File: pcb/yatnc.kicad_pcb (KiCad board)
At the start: 2 copper layers, 55 x 85 mm, 44 parts, among them J1 Conn_02x03_Top_Bottom, J2 JST, J3 Conn_01x02_Socket, J4 DFR0570, J5 Conn_01x13_Socket, J6 Conn_01x13_Socket, Q1 BC547, Q2 BC547, SW1 RST, U1 MAX3232

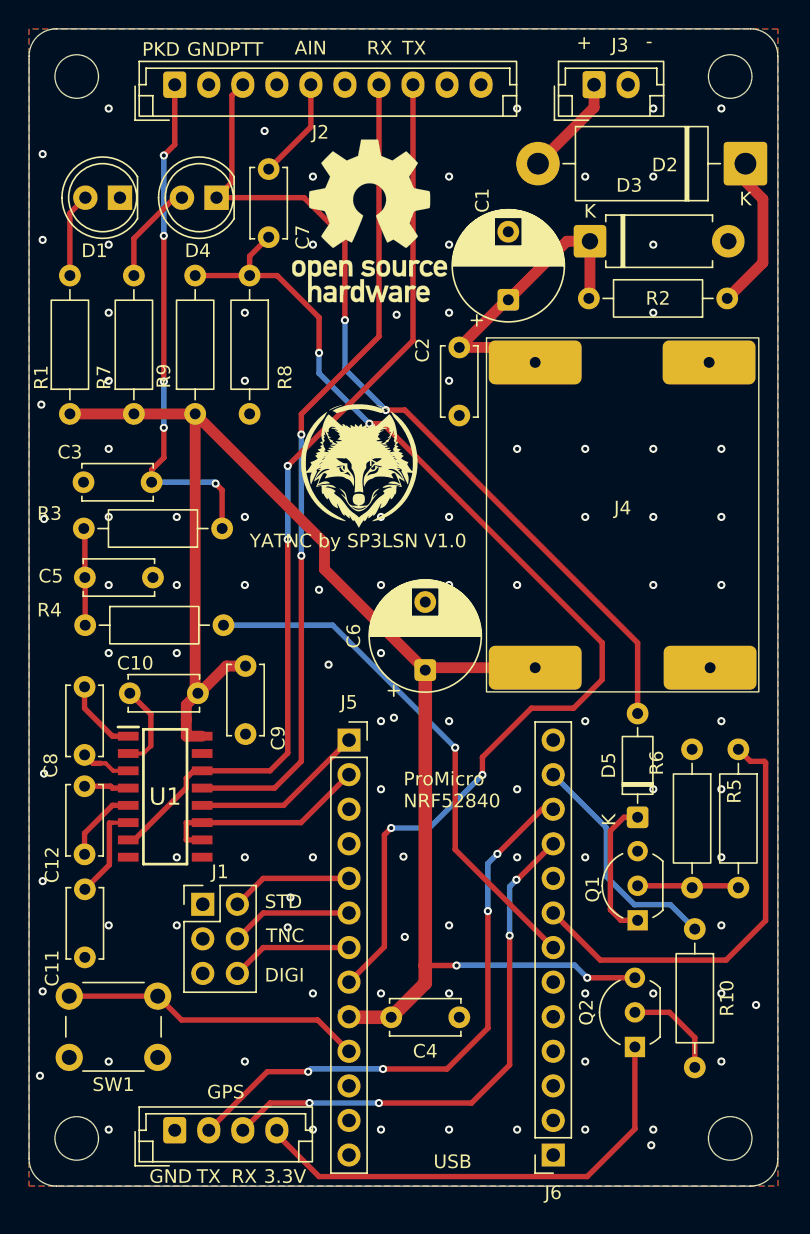
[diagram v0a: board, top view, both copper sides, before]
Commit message: max3232 refactor
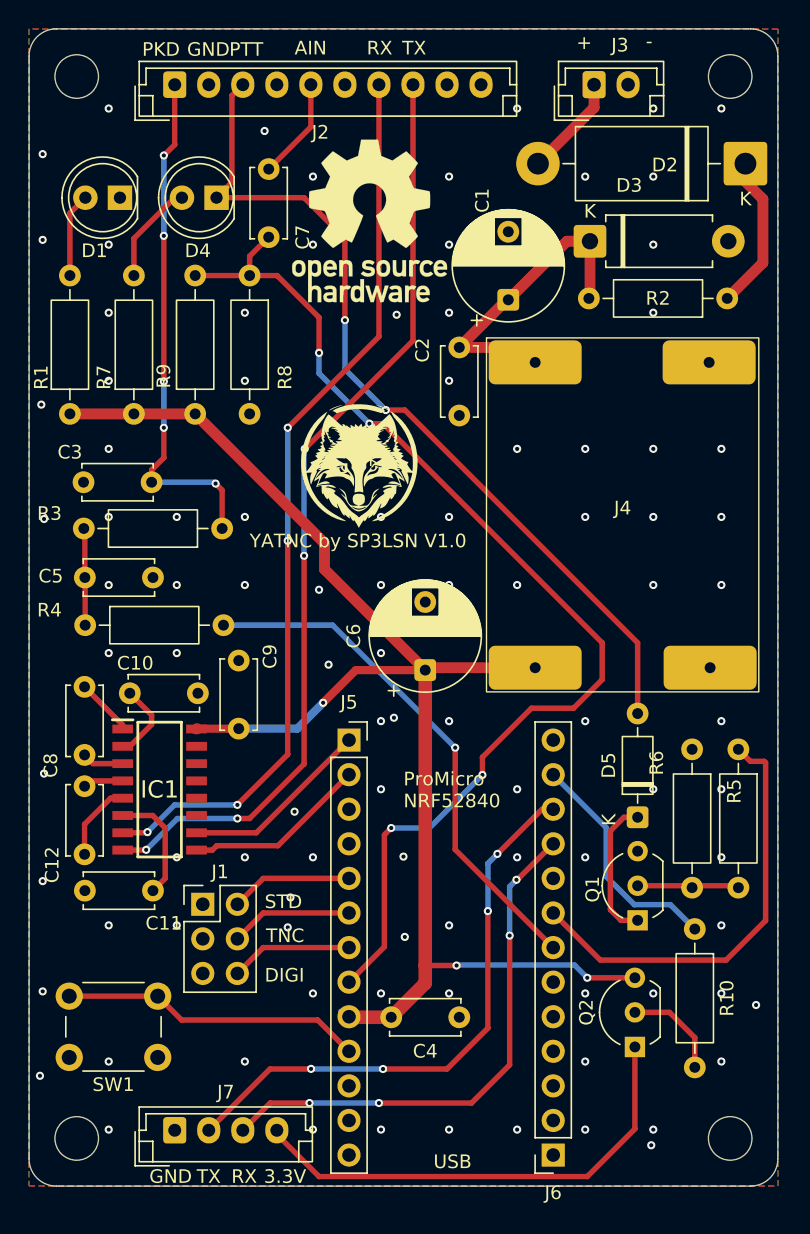
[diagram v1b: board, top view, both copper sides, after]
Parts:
- removed U1: MAX3232, liby:SOIC127P600X175-16N
- added IC1: MAX3232CDR, liby:SOIC127P600X175-16N, F.Cu at (180.1, 102.4)
- J7: renamed from GPS; value GPS -> Conn_01x04_Pin
- moved C9 4.63 mm to (185.9, 97.9), turned to 90 degrees
- moved C11 0.10 mm to (174.6, 109.8), turned to 0 degrees
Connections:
- net Net-(J6-Pin_8) renamed PTT ON
- C10 pad 2: 3.3V -> GND
- C11 pad 1: Net-(U1-VS-) -> GND
- C11 pad 2: GND -> Net-(IC1-V-)
- J5 pad 1: Net-(J5-Pin_1) -> U0_RX
- J5 pad 2: Net-(J5-Pin_2) -> U0_TX
- J6 pad 4: unconnected-(J6-Pin_4-Pad4) -> GND
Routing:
- net Net-(J5-Pin_2): track 15.8 -> 0.00 mm
- net U0_RX: track 0.00 -> 14.2 mm
- net U0_TX: track 0.00 -> 13.5 mm
- net Net-(J5-Pin_1): track 12.8 -> 0.00 mm
- net 3.3V: track 118.9 -> 107.9 mm, vias 2 -> 3
- net Net-(IC1-V-): track 0.00 -> 8.48 mm
- net Net-(U1-VS-): track 7.03 -> 0.00 mm
- net RX: track 60.2 -> 66.5 mm, vias 2 -> 4
- net TX: track 67.7 -> 69.2 mm, vias 2 -> 4
- net Net-(IC1-C1+): track 5.64 -> 4.26 mm
- net Net-(IC1-V+): track 6.41 -> 5.75 mm
- net Net-(IC1-C1-): track 3.69 -> 3.07 mm
- net GND: track 0.00 -> 0.38 mm, vias 99 -> 100

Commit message: final polish before test order
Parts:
- TO TRCV: renamed from J2
- renumbered J3 to PWR
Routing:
- net GND: vias 100 -> 99

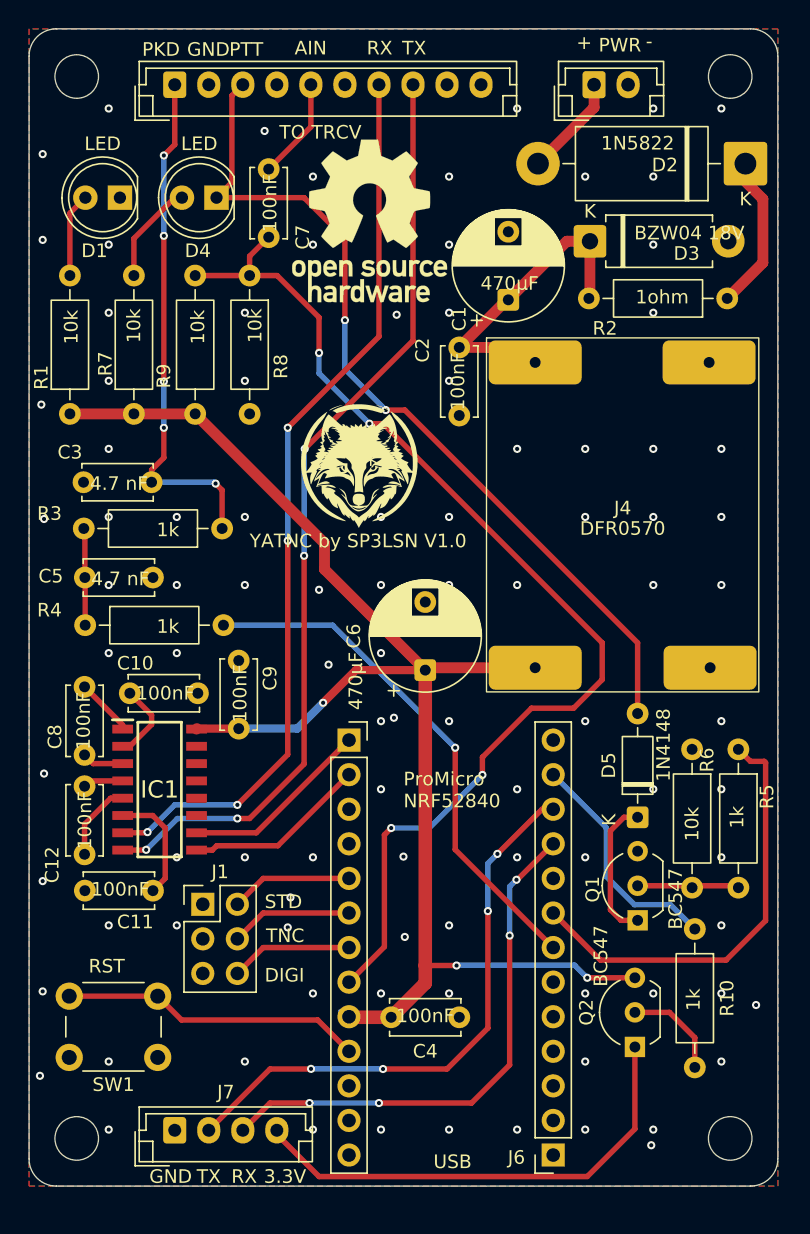
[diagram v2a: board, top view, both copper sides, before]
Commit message: small tweaks on silkscreen side, change components. update README, add bom
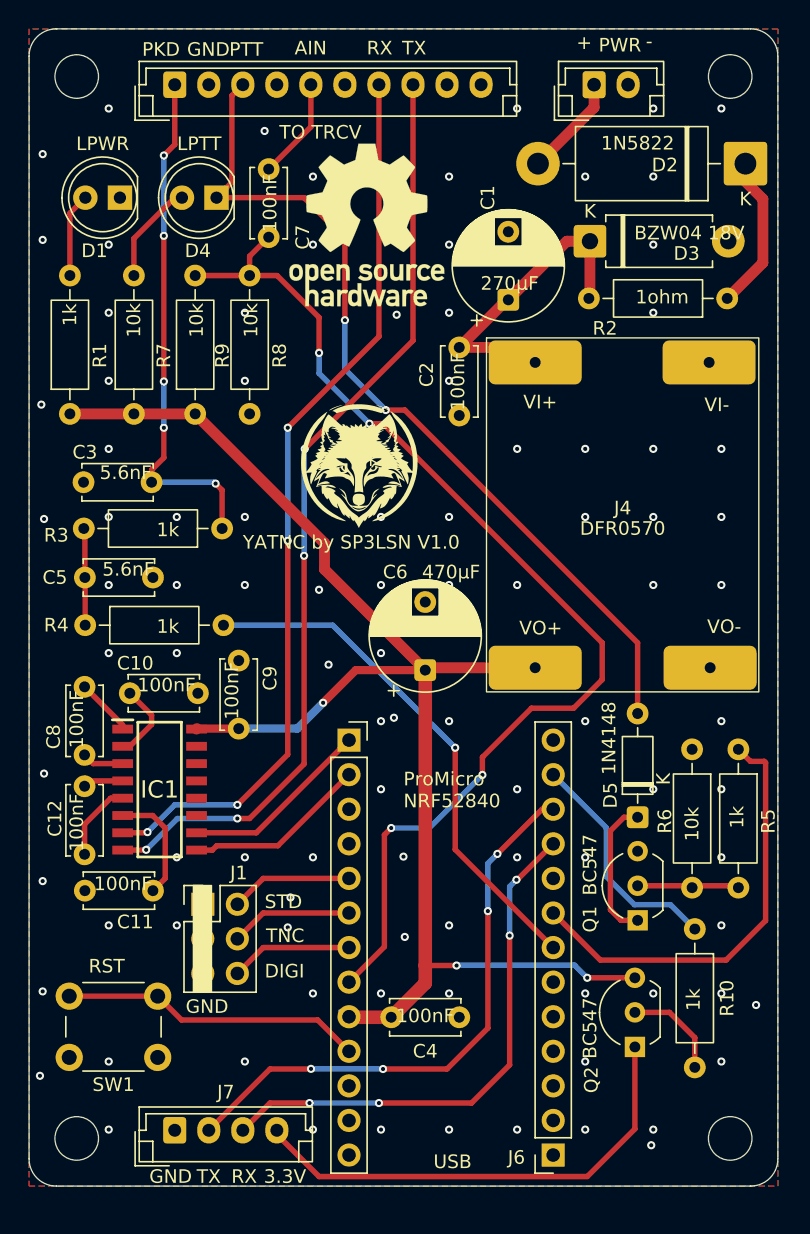
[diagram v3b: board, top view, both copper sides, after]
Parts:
- C1: value 470µF -> 270µF
- C3, C5: value 4.7 nF -> 5.6nF
- D1: value LED -> LPWR
- D4: value LED -> LPTT
- R1: value 10k -> 1k
- moved REF** 0.36 mm to (195.3, 60.9)
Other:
- board text added: "VI+"
- board text added: "VI-"
- board text added: "VO+"
- board text added: "VO-"
